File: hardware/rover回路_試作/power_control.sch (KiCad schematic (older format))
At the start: 16 parts

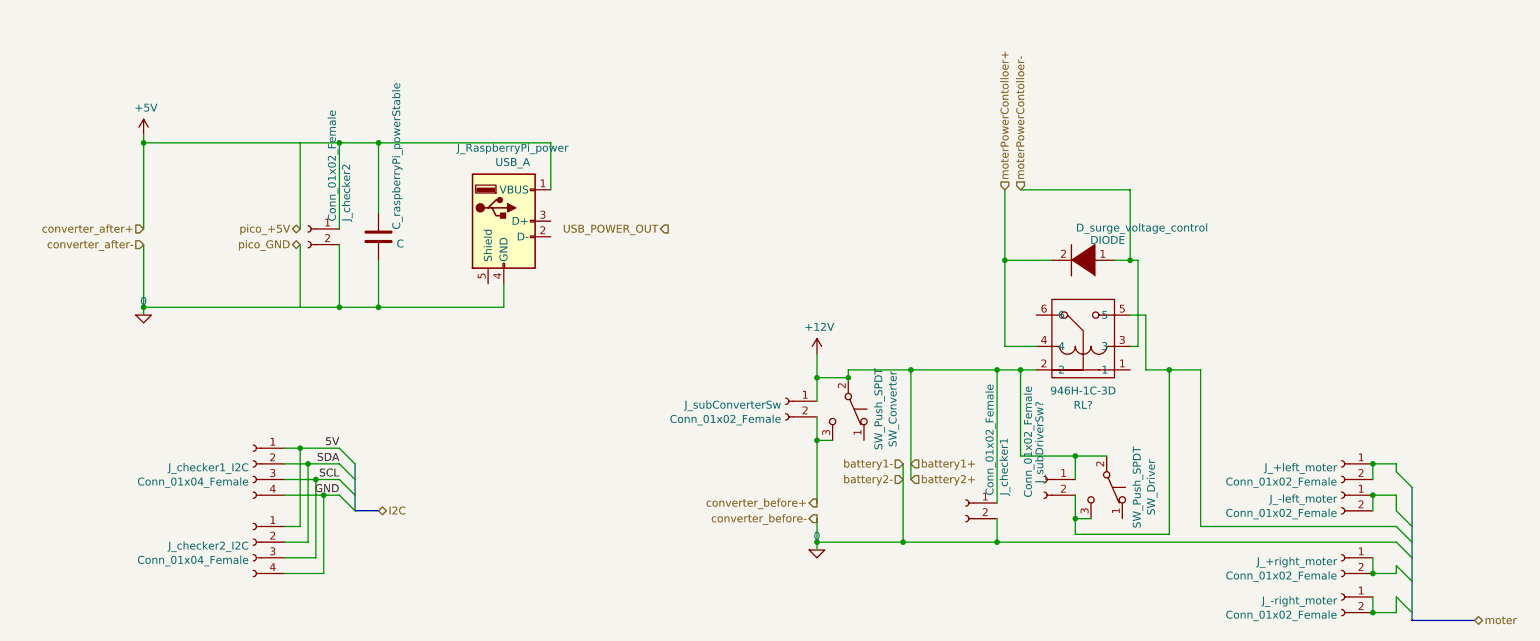
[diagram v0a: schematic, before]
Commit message: rover回路最終版v1.0 降圧回路に関してのみ未記載
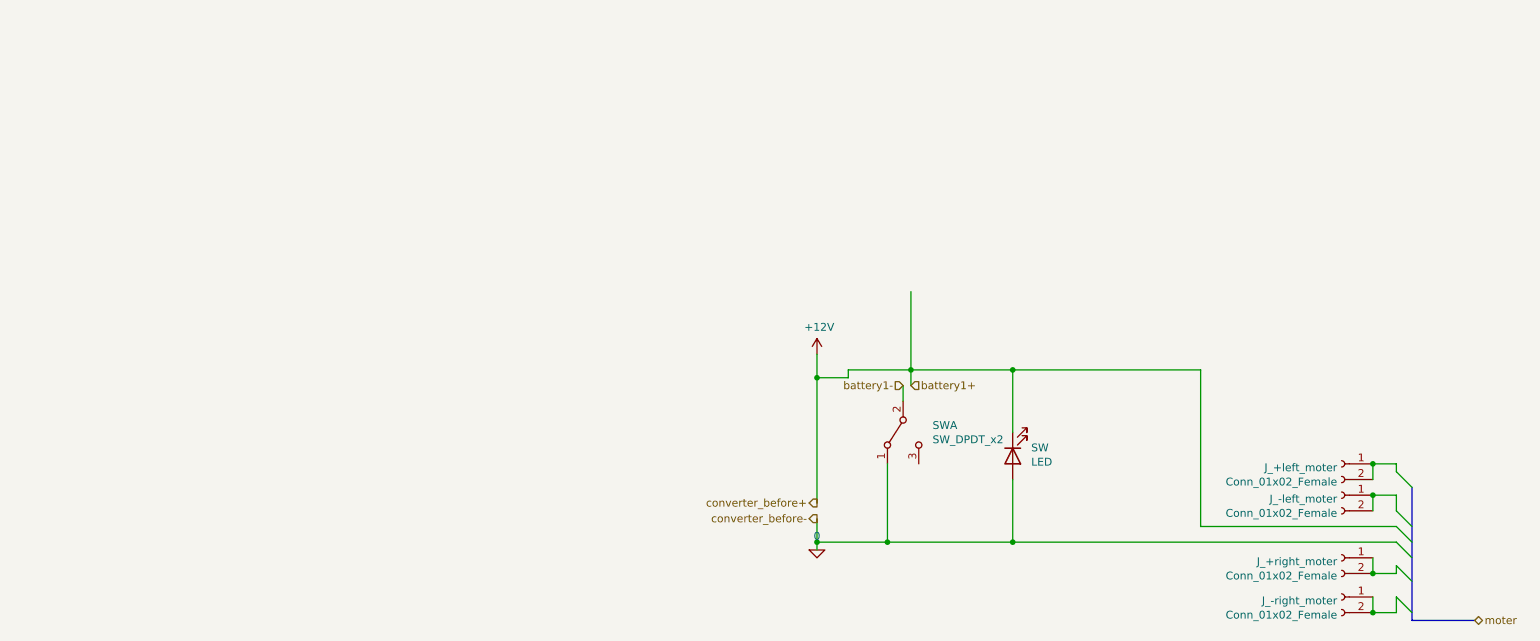
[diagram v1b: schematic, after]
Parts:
- removed C_raspberryPi_powerStable: C, symbol Device:C
- removed D_surge_voltage_control: DIODE, symbol pspice:DIODE
- removed J_RaspberryPi_power: USB_A, symbol Connector:USB_A
- removed J_checker1, J_checker2, J_subConverterSw, J_subDriverSw?: Conn_01x02_Female, symbol Connector:Conn_01x02_Female
- removed J_checker1_I2C, J_checker2_I2C: Conn_01x04_Female, symbol Connector:Conn_01x04_Female
- removed RL?: 946H-1C-3D, symbol My_Device:946H-1C-3D
- removed SW_Converter, SW_Driver: SW_Push_SPDT, symbol Switch:SW_Push_SPDT
- added SW: SW_DPDT_x2, symbol Switch:SW_DPDT_x2
- added SW: LED, symbol Device:LED
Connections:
- net labels removed: +5V, 5V, GND, I2C, SCL, SDA, USB_POWER_OUT, battery2+, battery2-, converter_after+, converter_after-, moterPowerContolloer+, moterPowerContolloer-, pico_+5V, pico_GND
- wire segments 91 -> 32
